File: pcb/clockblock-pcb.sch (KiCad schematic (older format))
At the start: 119 parts, among them IC1 TLC5971, IC2 TLC5971, IC3 TLC5971, IC4 PCF2129AT, IC5 TLV71333, IC6 ATTINY167, IC7 FT230X, J2 USB, P13 USBtoMAIN, P14 AVR_ISP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

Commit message: fabrication work
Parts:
- C25: footprint 0805(2012m)_tant-cap -> 1206(3216m)_tant-cap
- C27, R13: footprint ~ -> 0603(1608m)
- LED5: footprint ~ -> 0603(1608m)_led
- LND1, LND2, LND3, LND4: footprint TE_1551573-5_SPRING-FINGER -> 2x3MM_SM-PAD
- P13, P15: footprint 2x5-array -> 2x5-PIN-ARRAY_P100MIL_sm
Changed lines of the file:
@@
 Sheet 1 1
 Title "clockblock pcb"
-Date "9 nov 2013"
+Date "10 nov 2013"
 Rev "0.2"
 Comp "Wiley Cousins, LLC."
@@
 F 0 "C25" V 8150 4450 60  0000 C CNN
 F 1 "4.7uF" V 8050 4400 60  0000 C CNN
-F 2 "0805(2012m)_tant-cap" H 7750 4500 60  0001 C CNN
+F 2 "1206(3216m)_tant-cap" H 7750 4500 60  0001 C CNN
 F 3 "~" H 7750 4500 60  0001 C CNN
 F 4 "Kemet" H 7750 4500 60  0001 C CNN "Manufacturer"
@@
 F 0 "P13" H 7800 6100 60  0000 C CNN
 F 1 "USBtoMAIN" H 8400 6100 60  0000 C CNN
-F 2 "2x5-array" H 8050 6400 60  0001 C CNN
+F 2 "2x5-PIN-ARRAY_P100MIL_sm" H 8050 6400 60  0001 C CNN
 F 3 "~" H 8050 6400 60  0001 C CNN
 F 4 "CNC Tech" H 8050 6400 60  0001 C CNN "Manufacturer"
@@
 F 0 "P15" H 9250 6100 60  0000 C CNN
 F 1 "MAINtoUSB" H 9900 6100 60  0000 C CNN
-F 2 "2x5-array" H 9500 6400 60  0001 C CNN
+F 2 "2x5-PIN-ARRAY_P100MIL_sm" H 9500 6400 60  0001 C CNN
 F 3 "~" H 9500 6400 60  0001 C CNN
 F 4 "CNC Tech" H 9500 6400 60  0001 C CNN "Manufacturer"
@@
 E1 7A 30 2F E3 9E BF BB FC D0 5C 2F 77 12 1D A4 F0 58 02 39 97 10 5D 3F 53 4D 5C E7 C1 2F 96 BB
 0B B8 4B 44 66 C0 DD 9B E5 70 E1 99 33 E3 22 76 A6 C0 F5 70 86 E1 7A 3C 1F 00 F7 E2 62 F9 87 B5
-4B 6B 3B F8 7F 51 4C 22 23 01 FF ED 6E 00 00 00 00 49 45 4E 44 AE 42 60 82 00 $EndBitmap
+4B 6B 3B F8 7F 51 4C 22 23 01 FF ED 6E 00 00 00 00 49 45 4E 44 AE 42 60 82 16 $EndBitmap
 EndData
 $EndBitmap
@@
 00 00 80 1C 90 88 03 00 00 00 00 00 00 72 40 22 0E 00 00 00 00 00 00 C8 01 89 38 00 00 00 00 00
 00 20 07 24 E2 00 00 00 00 00 00 80 1C FC FF 3E 6A 41 A6 FA 5D A5 94 00 00 00 00 49 45 4E 44 AE
-42 60 82 38 $EndBitmap
+42 60 82 9C $EndBitmap
 EndData
 $EndBitmap
@@
 F 0 "LND1" H 4150 5100 60  0000 C CNN
 F 1 "VLED" H 4500 5200 60  0001 C CNN
-F 2 "TE_1551573-5_SPRING-FINGER" H 4300 5100 60  0001 C CNN
+F 2 "2x3MM_SM-PAD" H 4300 5100 60  0001 C CNN
 F 3 "~" H 4300 5100 60  0001 C CNN
 F 4 "N/A" H 4300 5100 60  0001 C CNN "Manufacturer"
@@
 F 0 "LND2" H 4150 5200 60  0000 C CNN
 F 1 "HOUR" H 4500 5300 60  0001 C CNN
-F 2 "TE_1551573-5_SPRING-FINGER" H 4300 5200 60  0001 C CNN
+F 2 "2x3MM_SM-PAD" H 4300 5200 60  0001 C CNN
 F 3 "~" H 4300 5200 60  0001 C CNN
 F 4 "N/A" H 4300 5200 60  0001 C CNN "Manufacturer"
@@
 F 0 "LND3" H 4150 5300 60  0000 C CNN
 F 1 "MIN" H 4500 5400 60  0001 C CNN
-F 2 "TE_1551573-5_SPRING-FINGER" H 4300 5300 60  0001 C CNN
+F 2 "2x3MM_SM-PAD" H 4300 5300 60  0001 C CNN
 F 3 "~" H 4300 5300 60  0001 C CNN
 F 4 "N/A" H 4300 5300 60  0001 C CNN "Manufacturer"
@@
 F 0 "LND4" H 4150 5400 60  0000 C CNN
 F 1 "SEC" H 4500 5500 60  0001 C CNN
-F 2 "TE_1551573-5_SPRING-FINGER" H 4300 5400 60  0001 C CNN
+F 2 "2x3MM_SM-PAD" H 4300 5400 60  0001 C CNN
 F 3 "~" H 4300 5400 60  0001 C CNN
 F 4 "N/A" H 4300 5400 60  0001 C CNN "Manufacturer"
@@
 F 0 "C27" V 4250 1550 60  0000 C CNN
 F 1 "0.1uF" V 4150 1600 60  0000 C CNN
-F 2 "~" H 4400 1450 60  0001 C CNN
+F 2 "0603(1608m)" H 4400 1450 60  0001 C CNN
 F 3 "~" H 4400 1450 60  0001 C CNN
 	1    4400 1450
@@
 F 0 "LED5" H 9000 5550 60  0000 C CNN
 F 1 "PWR" H 9250 5400 60  0000 C CNN
-F 2 "~" H 9150 5500 60  0001 C CNN
+F 2 "0603(1608m)_led" H 9150 5500 60  0001 C CNN
 F 3 "~" H 9150 5500 60  0001 C CNN
 	1    9150 5500
@@
 F 0 "R13" H 8700 5700 60  0000 C CNN
 F 1 "1kΩ" H 8700 5600 60  0000 C CNN
-F 2 "~" H 8750 5500 60  0001 C CNN
+F 2 "0603(1608m)" H 8750 5500 60  0001 C CNN
 F 3 "~" H 8750 5500 60  0001 C CNN
 	1    8750 5500

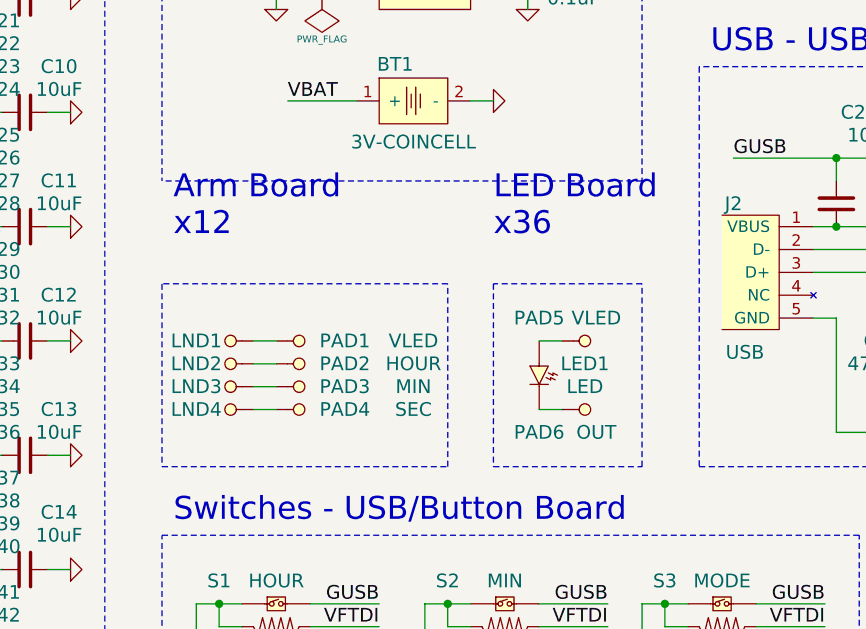
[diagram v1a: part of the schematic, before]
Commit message: changed schematic to 12 led arm boards
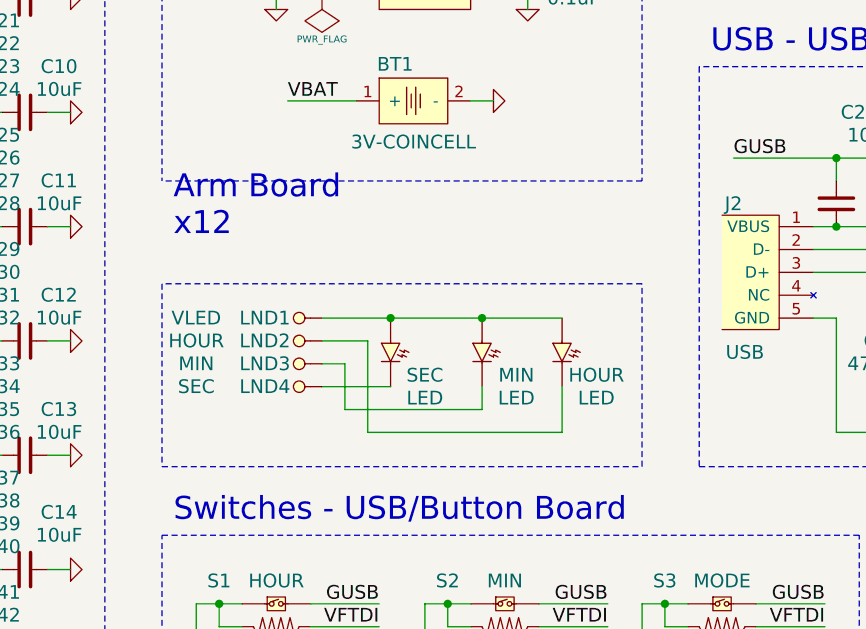
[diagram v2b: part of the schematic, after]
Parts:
- removed PAD1, PAD5: VLED, 3x5MM_SM-PAD, symbol TEST
- removed PAD2: HOUR, 3x5MM_SM-PAD, symbol TEST
- removed PAD3: MIN, 3x5MM_SM-PAD, symbol TEST
- removed PAD4: SEC, 3x5MM_SM-PAD, symbol TEST
- removed PAD6: OUT, 3x5MM_SM-PAD, symbol TEST
- added HOUR, MIN: LED, LED-5mm, symbol LED
- renumbered LED1 to SEC
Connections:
- net at SEC.1 (C): now also LND4.1 (TP)
- net at SEC.2 (A): now also LND1.1 (TP), HOUR.2 (A), MIN.2 (A)
- net at LND2.1 (TP): now also HOUR.1 (C)
- net at LND3.1 (TP): now also MIN.1 (C)
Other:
- note removed: "LED Board\nx36"
- moved on the sheet: LND1, LND2, LND3, LND4, SEC

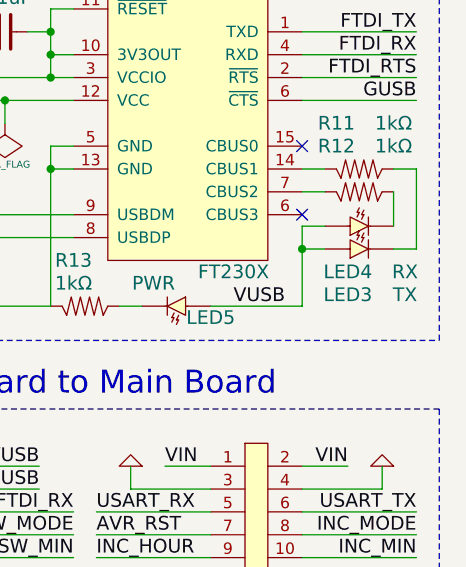
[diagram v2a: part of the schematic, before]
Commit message: switched TX abd RX labels in schematic. fixes #7
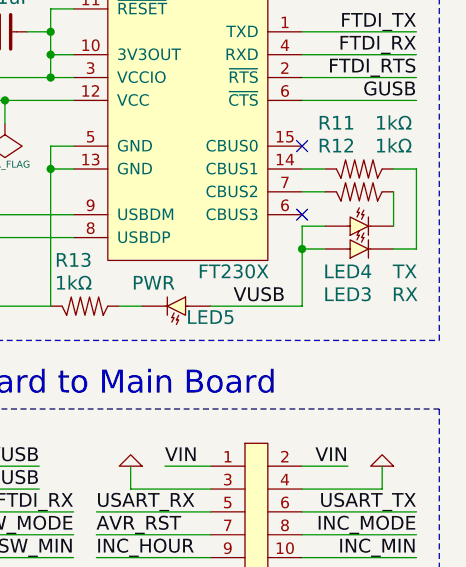
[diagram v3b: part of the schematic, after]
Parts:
- LED3: value TX -> RX
- LED4: value RX -> TX
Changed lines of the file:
@@
 P 9950 5250
 F 0 "LED3" H 9900 5050 60  0000 C CNN
-F 1 "TX" H 10150 5050 60  0000 C CNN
+F 1 "RX" H 10150 5050 60  0000 C CNN
 F 2 "0603(1608m)_led" H 9950 5250 60  0001 C CNN
 F 3 "~" H 9950 5250 60  0001 C CNN
@@
 P 9950 5150
 F 0 "LED4" H 9900 4950 60  0000 C CNN
-F 1 "RX" H 10150 4950 60  0000 C CNN
+F 1 "TX" H 10150 4950 60  0000 C CNN
 F 2 "0603(1608m)_led" H 9950 5150 60  0001 C CNN
 F 3 "~" H 9950 5150 60  0001 C CNN

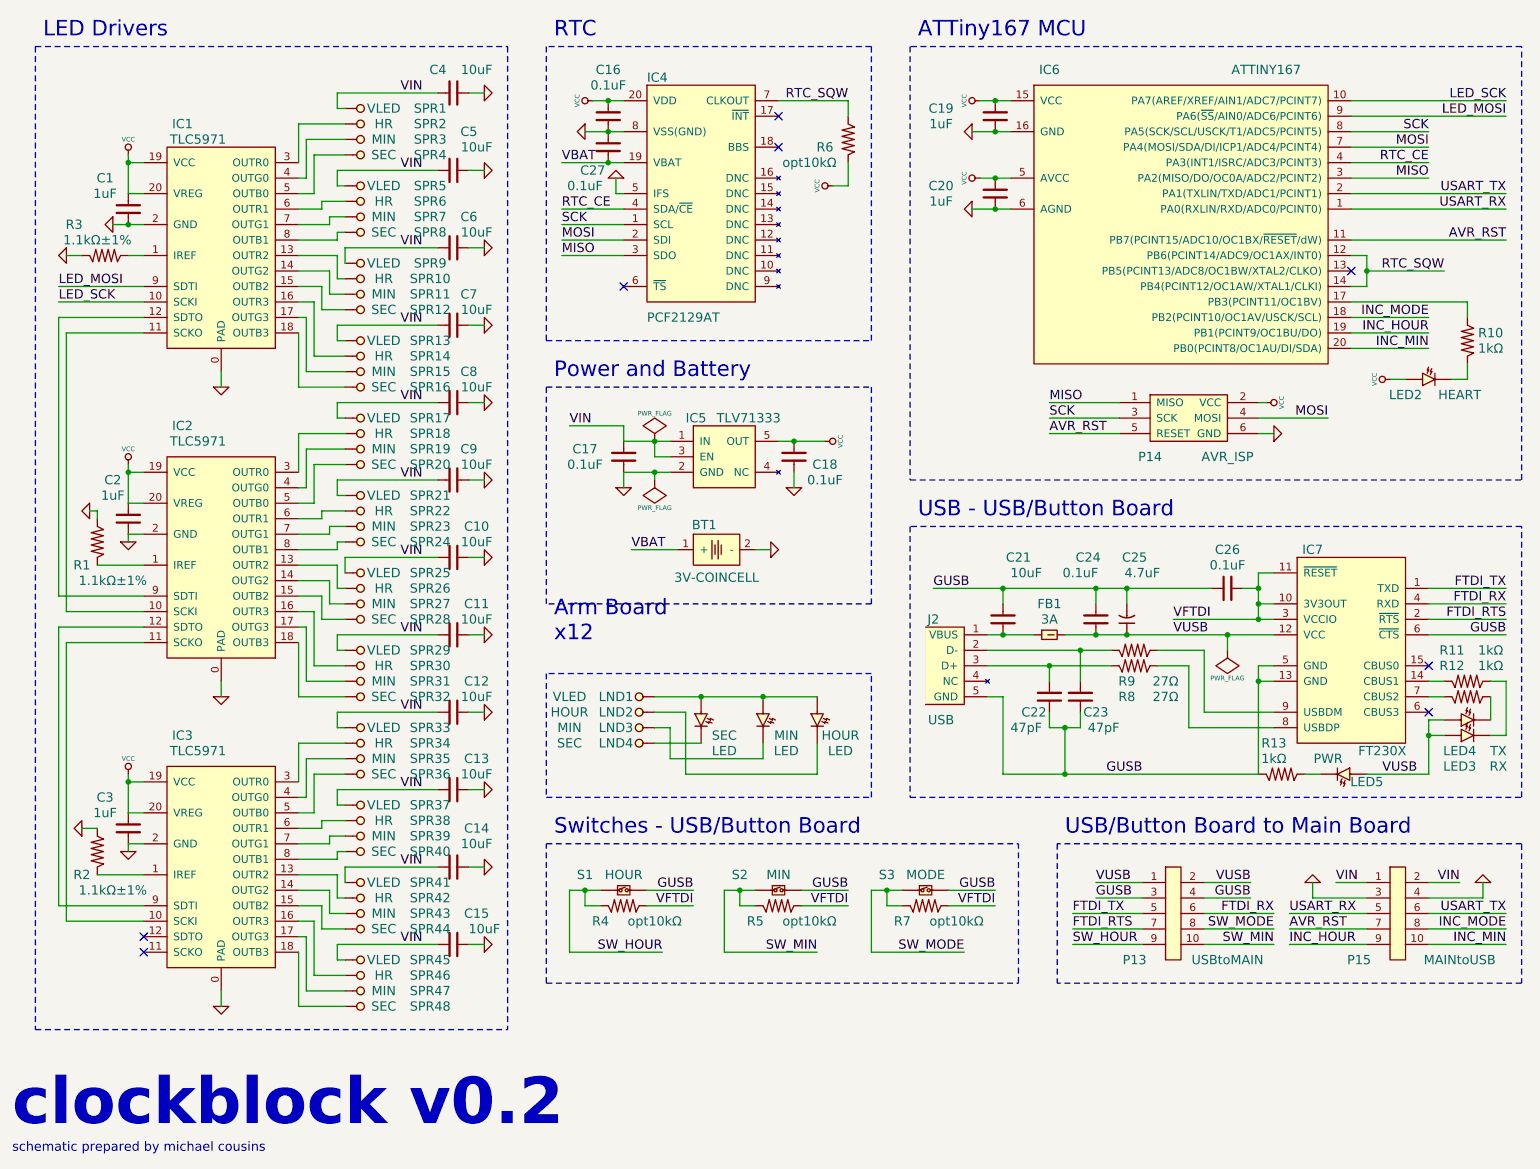
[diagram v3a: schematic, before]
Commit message: fixed dishonest capacitor values
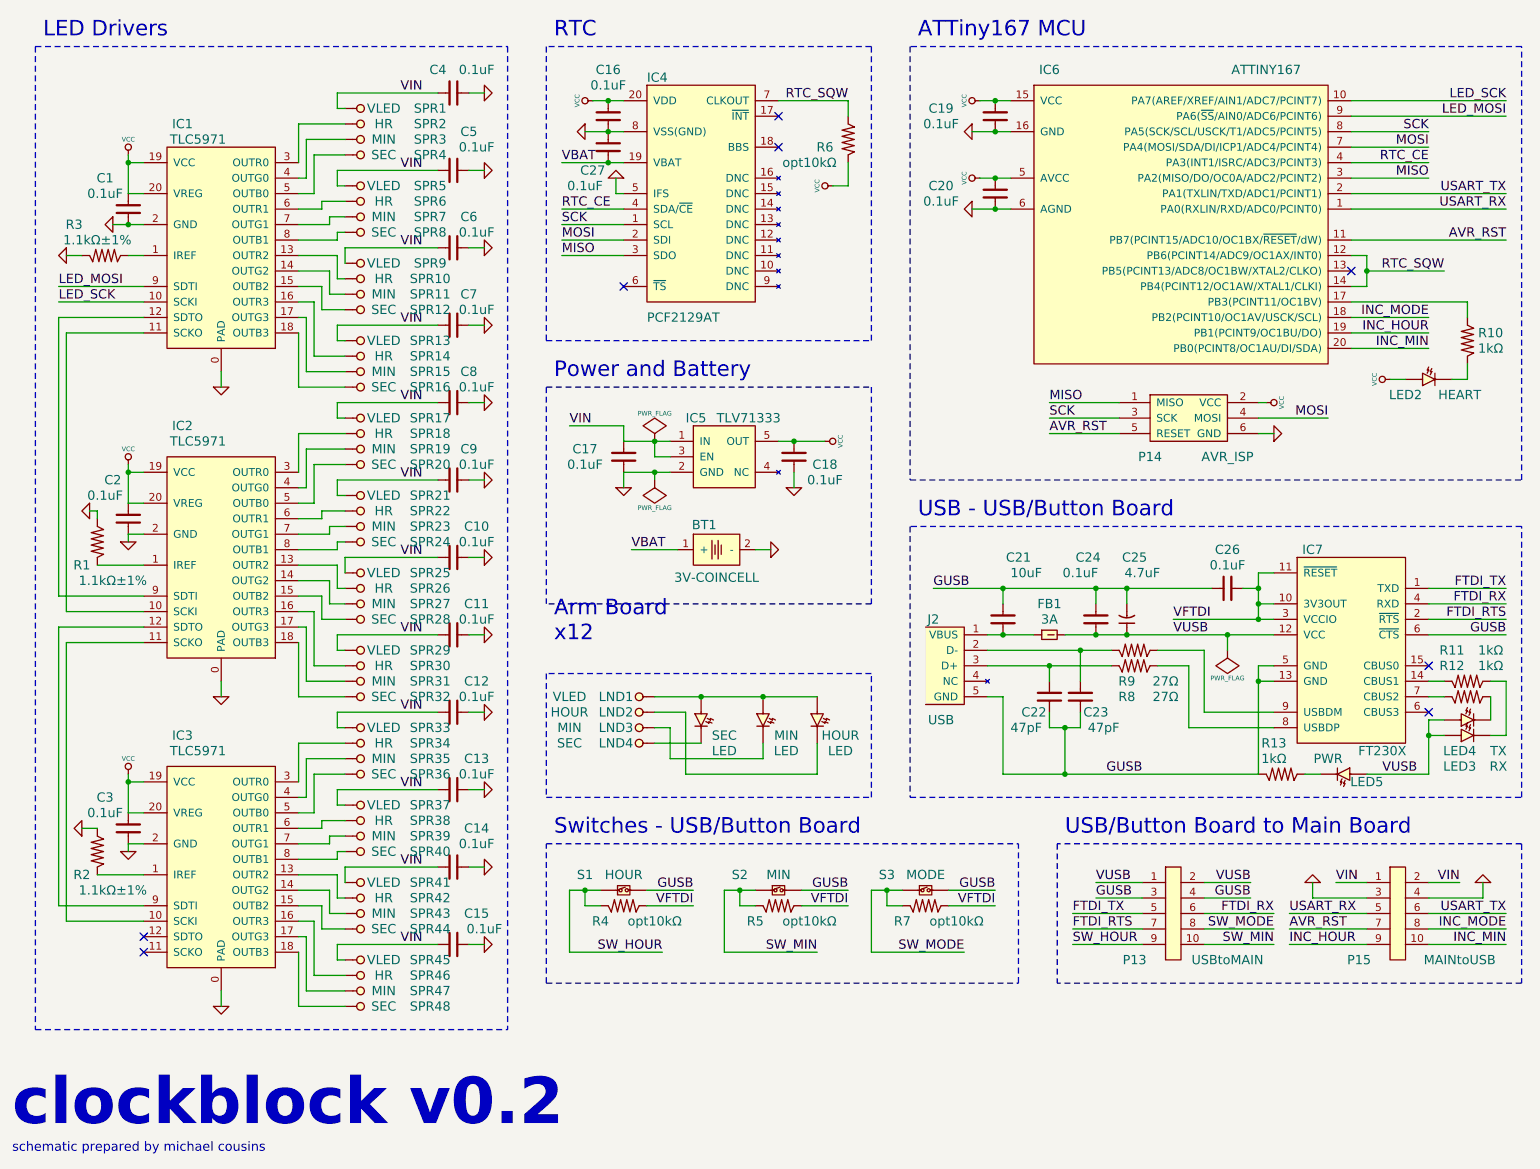
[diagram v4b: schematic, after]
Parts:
- C1, C19, C2, C20, C3: value 1uF -> 0.1uF
- C10, C11, C12, C13, C14, C15, C4, C5, C6, C7, C8, C9: value 10uF -> 0.1uF
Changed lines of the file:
@@
 P 6900 1250
 F 0 "C19" V 6850 900 60  0000 C CNN
-F 1 "1uF" V 6950 900 60  0000 C CNN
+F 1 "0.1uF" V 6950 900 60  0000 C CNN
 F 2 "0603(1608m)" H 6900 1250 60  0001 C CNN
 F 3 "~" H 6900 1250 60  0001 C CNN
@@
 P 6900 1750
 F 0 "C20" V 6850 1400 60  0000 C CNN
-F 1 "1uF" V 6950 1400 60  0000 C CNN
+F 1 "0.1uF" V 6950 1400 60  0000 C CNN
 F 2 "0603(1608m)" H 6900 1750 60  0001 C CNN
 F 3 "~" H 6900 1750 60  0001 C CNN
@@
 P 1300 5850
 F 0 "C3" V 1500 6000 60  0000 C CNN
-F 1 "1uF" V 1400 6000 60  0000 C CNN
+F 1 "0.1uF" V 1400 6000 60  0000 C CNN
 F 2 "0603(1608m)" H 1300 5850 60  0001 C CNN
 F 3 "~" H 1300 5850 60  0001 C CNN
@@
 P 1300 3850
 F 0 "C2" V 1550 3950 60  0000 C CNN
-F 1 "1uF" V 1450 3950 60  0000 C CNN
+F 1 "0.1uF" V 1450 4000 60  0000 C CNN
 F 2 "0603(1608m)" H 1300 3850 60  0001 C CNN
 F 3 "~" H 1300 3850 60  0001 C CNN
@@
 P 1300 1850
 F 0 "C1" V 1500 2000 60  0000 C CNN
-F 1 "1uF" V 1400 2000 60  0000 C CNN
+F 1 "0.1uF" V 1400 2000 60  0000 C CNN
 F 2 "0603(1608m)" H 1300 1850 60  0001 C CNN
 F 3 "~" H 1300 1850 60  0001 C CNN
@@
 P 3400 1600
 F 0 "C5" H 3500 1850 60  0000 C CNN
-F 1 "10uF" H 3550 1750 60  0000 C CNN
+F 1 "0.1uF" H 3550 1750 60  0000 C CNN
 F 2 "0603(1608m)" H 3400 1600 60  0001 C CNN
 F 3 "~" H 3400 1600 60  0001 C CNN
@@
 P 3400 2600
 F 0 "C7" H 3500 2800 60  0000 C CNN
-F 1 "10uF" H 3550 2700 60  0000 C CNN
+F 1 "0.1uF" H 3550 2700 60  0000 C CNN
 F 2 "0603(1608m)" H 3400 2600 60  0001 C CNN
 F 3 "~" H 3400 2600 60  0001 C CNN
@@
 P 3400 2100
 F 0 "C6" H 3500 2300 60  0000 C CNN
-F 1 "10uF" H 3550 2200 60  0000 C CNN
+F 1 "0.1uF" H 3550 2200 60  0000 C CNN
 F 2 "0603(1608m)" H 3400 2100 60  0001 C CNN
 F 3 "~" H 3400 2100 60  0001 C CNN
@@
 P 3400 1100
 F 0 "C4" H 3300 1250 60  0000 C CNN
-F 1 "10uF" H 3550 1250 60  0000 C CNN
+F 1 "0.1uF" H 3550 1250 60  0000 C CNN
 F 2 "0603(1608m)" H 3400 1100 60  0001 C CNN
 F 3 "~" H 3400 1100 60  0001 C CNN
@@
 P 3400 3600
 F 0 "C9" H 3500 3800 60  0000 C CNN
-F 1 "10uF" H 3550 3700 60  0000 C CNN
+F 1 "0.1uF" H 3550 3700 60  0000 C CNN
 F 2 "0603(1608m)" H 3400 3600 60  0001 C CNN
 F 3 "~" H 3400 3600 60  0001 C CNN
@@
 P 3400 4600
 F 0 "C11" H 3550 4800 60  0000 C CNN
-F 1 "10uF" H 3550 4700 60  0000 C CNN
+F 1 "0.1uF" H 3550 4700 60  0000 C CNN
 F 2 "0603(1608m)" H 3400 4600 60  0001 C CNN
 F 3 "~" H 3400 4600 60  0001 C CNN
@@
 P 3400 4100
 F 0 "C10" H 3550 4300 60  0000 C CNN
-F 1 "10uF" H 3550 4200 60  0000 C CNN
+F 1 "0.1uF" H 3550 4200 60  0000 C CNN
 F 2 "0603(1608m)" H 3400 4100 60  0001 C CNN
 F 3 "~" H 3400 4100 60  0001 C CNN
@@
 P 3400 3100
 F 0 "C8" H 3500 3300 60  0000 C CNN
-F 1 "10uF" H 3550 3200 60  0000 C CNN
+F 1 "0.1uF" H 3550 3200 60  0000 C CNN
 F 2 "0603(1608m)" H 3400 3100 60  0001 C CNN
 F 3 "~" H 3400 3100 60  0001 C CNN
@@
 P 3400 5600
 F 0 "C13" H 3550 5800 60  0000 C CNN
-F 1 "10uF" H 3550 5700 60  0000 C CNN
+F 1 "0.1uF" H 3550 5700 60  0000 C CNN
 F 2 "0603(1608m)" H 3400 5600 60  0001 C CNN
 F 3 "~" H 3400 5600 60  0001 C CNN
@@
 P 3400 6600
 F 0 "C15" H 3550 6800 60  0000 C CNN
-F 1 "10uF" H 3600 6700 60  0000 C CNN
+F 1 "0.1uF" H 3600 6700 60  0000 C CNN
 F 2 "0603(1608m)" H 3400 6600 60  0001 C CNN
 F 3 "~" H 3400 6600 60  0001 C CNN
@@
 P 3400 6100
 F 0 "C14" H 3550 6350 60  0000 C CNN
-F 1 "10uF" H 3550 6250 60  0000 C CNN
+F 1 "0.1uF" H 3550 6250 60  0000 C CNN
 F 2 "0603(1608m)" H 3400 6100 60  0001 C CNN
 F 3 "~" H 3400 6100 60  0001 C CNN
@@
 P 3400 5100
 F 0 "C12" H 3550 5300 60  0000 C CNN
-F 1 "10uF" H 3550 5200 60  0000 C CNN
+F 1 "0.1uF" H 3550 5200 60  0000 C CNN
 F 2 "0603(1608m)" H 3400 5100 60  0001 C CNN
 F 3 "~" H 3400 5100 60  0001 C CNN
@@
 E1 7A 30 2F E3 9E BF BB FC D0 5C 2F 77 12 1D A4 F0 58 02 39 97 10 5D 3F 53 4D 5C E7 C1 2F 96 BB
 0B B8 4B 44 66 C0 DD 9B E5 70 E1 99 33 E3 22 76 A6 C0 F5 70 86 E1 7A 3C 1F 00 F7 E2 62 F9 87 B5
-4B 6B 3B F8 7F 51 4C 22 23 01 FF ED 6E 00 00 00 00 49 45 4E 44 AE 42 60 82 05 $EndBitmap
+4B 6B 3B F8 7F 51 4C 22 23 01 FF ED 6E 00 00 00 00 49 45 4E 44 AE 42 60 82 15 $EndBitmap
 EndData
 $EndBitmap
@@
 00 00 80 1C 90 88 03 00 00 00 00 00 00 72 40 22 0E 00 00 00 00 00 00 C8 01 89 38 00 00 00 00 00
 00 20 07 24 E2 00 00 00 00 00 00 80 1C FC FF 3E 6A 41 A6 FA 5D A5 94 00 00 00 00 49 45 4E 44 AE
-42 60 82 BB $EndBitmap
+42 60 82 79 $EndBitmap
 EndData
 $EndBitmap
